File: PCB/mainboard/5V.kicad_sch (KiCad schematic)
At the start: 8 parts, among them U1 TPS5430DDA

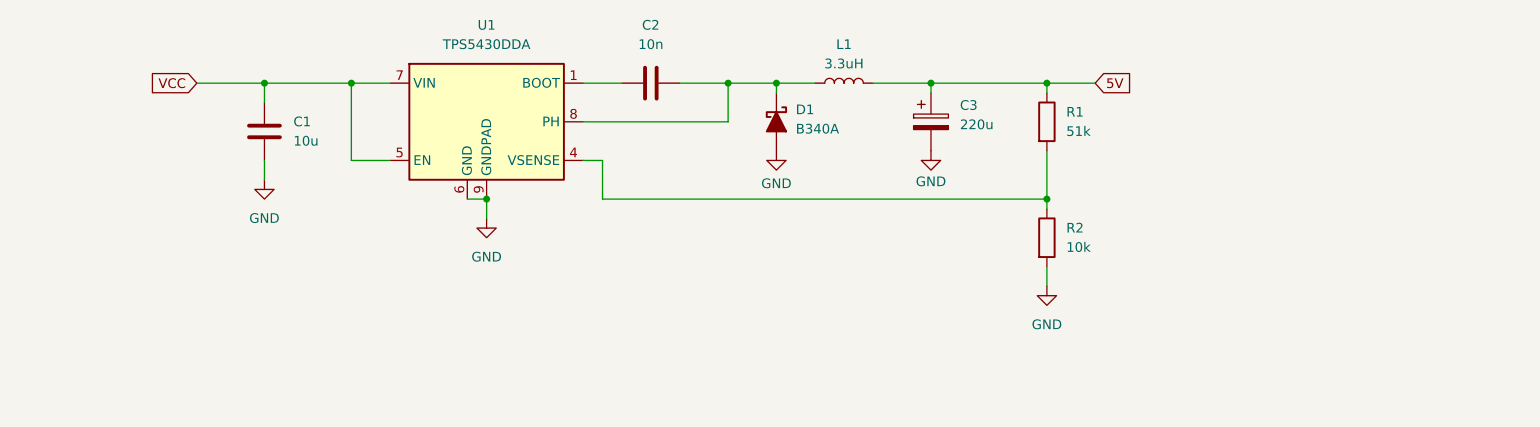
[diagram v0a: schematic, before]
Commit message: upgrades to STM32 Board
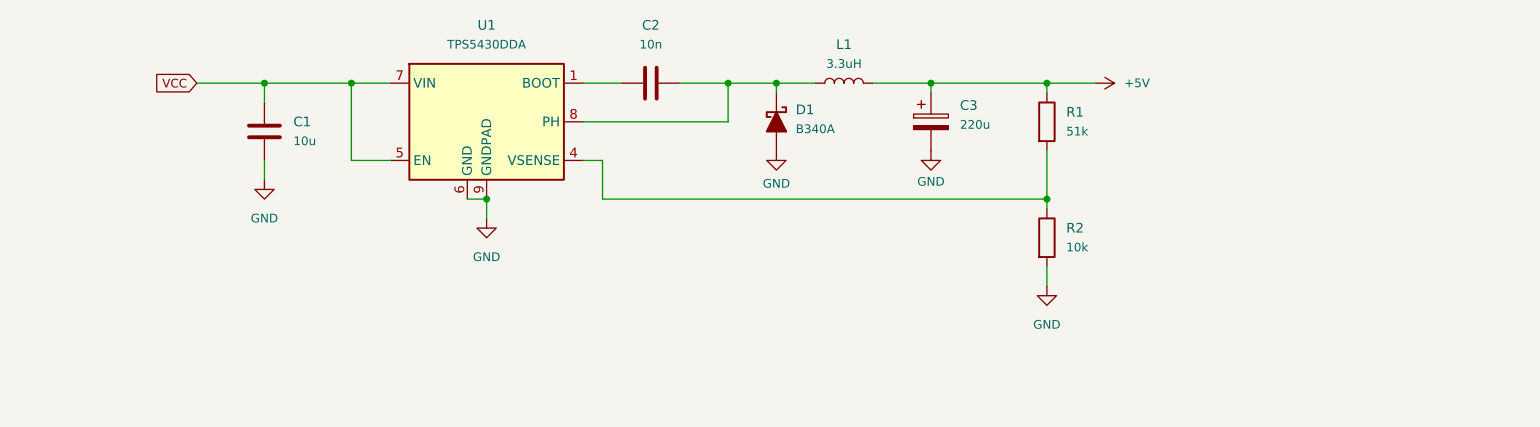
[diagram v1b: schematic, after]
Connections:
- net 5V renamed +5V
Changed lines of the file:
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@@
 		(effects
 			(font
-				(size 1.27 1.27)
+				(size 1.143 1.143)
 			)
 			(justify right)
@@
 		)
 	)
-	(global_label "5V"
-		(shape input)
-		(at 208.28 78.74 0)
-		(fields_autoplaced yes)
-		(effects
-			(font
-				(size 1.27 1.27)
-			)
-			(justify left)
-		)
-		(property "Intersheetrefs" "${INTERSHEET_REFS}"
-			(at 213.5633 78.74 0)
-			(effects
-				(font
-					(size 1.27 1.27)
-				)
-				(justify left)
-				(hide yes)
-			)
-		)
-	)
 	(symbol
 		(lib_id "power:GND")
@@
 			(effects
 				(font
-					(size 1.27 1.27)
+					(size 1.143 1.143)
 				)
 			)
@@
 			(effects
 				(font
-					(size 1.27 1.27)
+					(size 1.143 1.143)
 				)
 				(justify left)
@@
 			(effects
 				(font
-					(size 1.27 1.27)
+					(size 1.143 1.143)
 				)
 			)
@@
 			(effects
 				(font
-					(size 1.27 1.27)
+					(size 1.143 1.143)
 				)
 			)
@@
 			(effects
 				(font
-					(size 1.27 1.27)
+					(size 1.143 1.143)
 				)
 			)
@@
 			(effects
 				(font
-					(size 1.27 1.27)
+					(size 1.143 1.143)
 				)
 			)
@@
 			(effects
 				(font
-					(size 1.27 1.27)
+					(size 1.143 1.143)
 				)
 			)
@@
 			(effects
 				(font
-					(size 1.27 1.27)
+					(size 1.143 1.143)
 				)
 				(justify left)
@@
 			(effects
 				(font
-					(size 1.27 1.27)
+					(size 1.143 1.143)
 				)
 			)
@@
 			(effects
 				(font
-					(size 1.27 1.27)
+					(size 1.143 1.143)
 				)
 			)
@@
 			(effects
 				(font
-					(size 1.27 1.27)
+					(size 1.143 1.143)
 				)
 				(justify right)
@@
 			(effects
 				(font
-					(size 1.27 1.27)
+					(size 1.143 1.143)
 				)
 				(justify left)
@@
 	)
 	(symbol
+		(lib_id "power:+5V")
+		(at 208.28 78.74 270)
+		(unit 1)
+		(exclude_from_sim no)
+		(in_bom yes)
+		(on_board yes)
+		(dnp no)
+		(fields_autoplaced yes)
+		(property "Reference" "#PWR0101"
+			(at 204.47 78.74 0)
+			(effects
+				(font
+					(size 1.27 1.27)
+				)
+				(hide yes)
+			)
+		)
+		(property "Value" "+5V"
+			(at 212.09 78.7399 90)
+			(effects
+				(font
+					(size 1.143 1.143)
+				)
+				(justify left)
+			)
+		)
+		(property "Footprint" ""
+			(at 208.28 78.74 0)
+			(effects
+				(font
+					(size 1.27 1.27)
+				)
+				(hide yes)
+			)
+		)
+		(property "Datasheet" ""
+			(at 208.28 78.74 0)
+			(effects
+				(font
+					(size 1.27 1.27)
+				)
+				(hide yes)
+			)
+		)
+		(property "Description" "Power symbol creates a global label with name \"+5V\""
+			(at 208.28 78.74 0)
+			(effects
+				(font
+					(size 1.27 1.27)
+				)
+				(hide yes)
+			)
+		)
+		(pin "1"
+		)
+		(instances
+			(project ""
+				(path "/d49cf26c-5888-451d-a9f9-a714323b15a2/bdbd02e8-c901-46b8-afbc-38e96523b127"
+					(reference "#PWR0101")
+					(unit 1)
+				)
+			)
+		)
+	)
+	(symbol
 		(lib_id "Device:C")
 		(at 99.06 85.09 0)
@@
 			(effects
 				(font
-					(size 1.27 1.27)
+					(size 1.143 1.143)
 				)
 				(justify left)

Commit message: Made the Mainboard BCP Part Layout
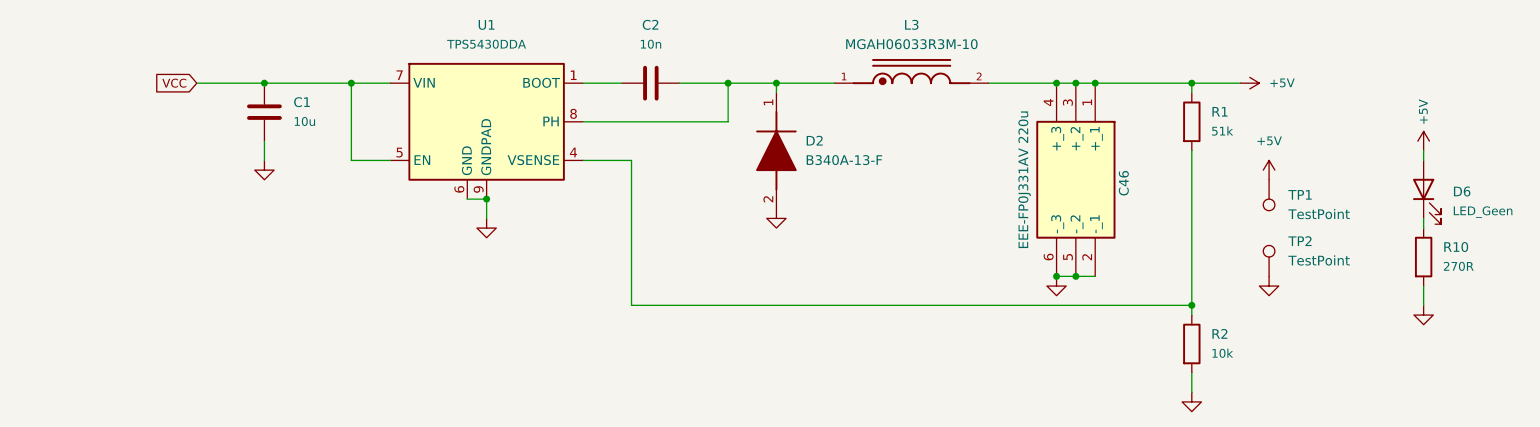
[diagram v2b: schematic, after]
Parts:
- removed C3: 220u, lib:EEEFP0J331AV, symbol Device:C_Polarized
- removed D1: B340A, PCM_Diode_SMD_AKL:D_SMA, symbol PCM_Diode_Schottky_AKL:B340A
- removed L1: 3.3uH, lib:IND_MGAH06033R3M-10, symbol Device:L
- added C46: EEE-FP0J331AV 220u, lib:EEEFP0J331AV, symbol EEE-FP0J331AV:EEE-FP0J331AV
- added D2: B340A-13-F, lib:DIOM5226X240N, symbol B340A-13-F:B340A-13-F
- added D6: LED_Geen, lib:LEDC1608X70N, symbol Device:LED
- added L3: MGAH06033R3M-10, lib:IND_MGAH06033R3M-10, symbol MGAH06033R3M-10:MGAH06033R3M-10
- added R10: 270R, Resistor_SMD:R_0201_0603Metric_Pad0.64x0.40mm_HandSolder, symbol Device:R
- added TP1, TP2: TestPoint, TestPoint:TestPoint_Pad_D2.0mm, symbol Connector:TestPoint
- R1, R2: footprint Resistor_SMD:R_0201_0603Metric_Pad0.64x0.40mm_HandSolder -> Resistor_SMD:R_0402_1005Metric_Pad0.72x0.64mm_HandSolder
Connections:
- net +5V: now also C46.1 (+_1), C46.3 (+_2), C46.4 (+_3), D6.2 (A), L3.2, TP1.1
- net GND: now also C46.2 (-_1), C46.5 (-_2), C46.6 (-_3), D2.2 (A), R10.2, TP2.1
- net at C2.2, U1.8 (PH): now also D2.1 (K), L3.1
- new net: D6.1 (K), R10.1
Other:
- moved on the sheet: R1, R2

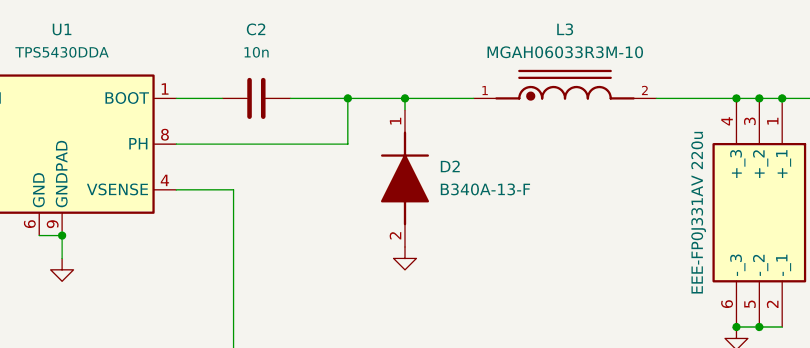
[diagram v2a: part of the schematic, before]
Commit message: Stop tracking renders folder & final Powerstrip and Mainboard PCB
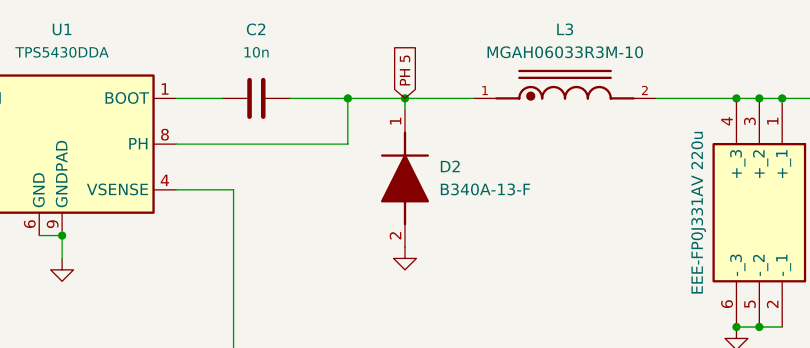
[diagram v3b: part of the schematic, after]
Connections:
- net PH 5: now reaches C2.2, D2.1 (K), L3.1, U1.8 (PH)
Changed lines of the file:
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@@
+		)
+	)
+	(global_label "PH 5"
+		(shape input)
+		(at 166.37 78.74 90)
+		(fields_autoplaced yes)
+		(effects
+			(font
+				(size 1.143 1.143)
+			)
+			(justify left)
+		)
+		(property "Intersheetrefs" "${INTERSHEET_REFS}"
+			(at 166.37 71.7536 90)
+			(effects
+				(font
+					(size 1.27 1.27)
+				)
+				(justify left)
+				(hide yes)
+			)
 		)
 	)

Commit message: random upload
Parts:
- removed C1: 10u, Capacitor_SMD:C_1206_3216Metric_Pad1.33x1.80mm_HandSolder, symbol Device:C
- removed C2: 10n, Capacitor_SMD:C_1206_3216Metric_Pad1.33x1.80mm_HandSolder, symbol Device:C
- removed C46: EEE-FP0J331AV 220u, lib:EEEFP0J331AV, symbol EEE-FP0J331AV:EEE-FP0J331AV
- removed D2: B340A-13-F, lib:DIOM5226X240N, symbol B340A-13-F:B340A-13-F
- removed L3: MGAH06033R3M-10, lib:IND_MGAH06033R3M-10, symbol MGAH06033R3M-10:MGAH06033R3M-10
- removed R1: 51k, Resistor_SMD:R_0402_1005Metric_Pad0.72x0.64mm_HandSolder, symbol Device:R
- removed R2: 10k, Resistor_SMD:R_0402_1005Metric_Pad0.72x0.64mm_HandSolder, symbol Device:R
- removed U1: TPS5430DDA, Package_SO:TI_SO-PowerPAD-8_ThermalVias, symbol Regulator_Switching:TPS5430DDA
- added C46: 33u, lib:C4532_Commercial, symbol Device:C
- added C47: 10n, Capacitor_SMD:C_0402_1005Metric_Pad0.74x0.62mm_HandSolder, symbol Device:C
- added C48: 100n, Capacitor_SMD:C_0402_1005Metric_Pad0.74x0.62mm_HandSolder, symbol Device:C
- added C49: 10u, Capacitor_SMD:C_0402_1005Metric_Pad0.74x0.62mm_HandSolder, symbol Device:C
- added C6: 22p, Capacitor_SMD:C_0402_1005Metric_Pad0.74x0.62mm_HandSolder, symbol Device:C
- added R29: 27.4k, Resistor_SMD:R_0402_1005Metric_Pad0.72x0.64mm_HandSolder, symbol Device:R
- added R33: 10k, Resistor_SMD:R_0402_1005Metric_Pad0.72x0.64mm_HandSolder, symbol Device:R
- added R34: 135k, Resistor_SMD:R_0402_1005Metric_Pad0.72x0.64mm_HandSolder, symbol Device:R
- added R44: 30k, Resistor_SMD:R_0402_1005Metric_Pad0.72x0.64mm_HandSolder, symbol Device:R
- added VR1: TPSM863252RDXR, lib:VREG_TPSM863252RDXR, symbol TPSM863252RDXR:TPSM863252RDXR
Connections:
- net +5V: now also C46.1, C6.1, R34.1, VR1.3 (VOUT)
- net GND: now also C46.2, C47.2, C48.2, C49.2, R33.2, R44.2, VR1.4 (PGND)
- net VCC: now also C48.1, C49.1, R29.1, VR1.1 (VIN)
- new net: C47.1, R29.2, R33.1, VR1.6 (EN)
- new net: C6.2, R34.2, R44.1, VR1.7 (FB)
- no-connect marks 0 -> 1
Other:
- note added: "5.8V-8.4V to 3.3V @ 2A"
- moved on the sheet: D6, R10, TP1, TP2
